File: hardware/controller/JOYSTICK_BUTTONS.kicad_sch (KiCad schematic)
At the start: 0 parts

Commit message: asdasd
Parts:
- added J2, J3: Joystick, SamacSys_Parts:SparkfunJoystick, symbol SamacSys_Parts:Joystick_Sparkfun_COM-09032
- added R1, R2, R3, R4, R5, R6: 10k, RESC2012X60N, symbol Device:R
- added SW1: UP, SamacSys_Parts:SW_PUSH_6mm, symbol ECE319K:SW_Push
- added SW2: LEFT, SamacSys_Parts:SW_PUSH_6mm, symbol ECE319K:SW_Push
- added SW3: DOWN, SamacSys_Parts:SW_PUSH_6mm, symbol ECE319K:SW_Push
- added SW4: RGHT, SamacSys_Parts:SW_PUSH_6mm, symbol ECE319K:SW_Push
- added SW5: BOOT, SamacSys_Parts:SW_PUSH_6mm, symbol Switch:SW_Push
- added SW6: RESET, SamacSys_Parts:SW_PUSH_6mm, symbol Switch:SW_Push
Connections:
- new net +3V3: J2.3 (V+), J2.4 (H+), J3.3 (V+), J3.4 (H+), SW1.2, SW2.2, SW3.2, SW4.2, SW5.2, SW6.2
- new net BUT_BOOT: R5.1, SW5.1
- new net BUT_DWN: R3.1, SW3.1
- new net BUT_LFT: R2.1, SW2.1
- new net BUT_RHT: R4.1, SW4.1
- new net BUT_RST: R6.1, SW6.1
- new net BUT_UP: R1.1, SW1.1
- new net GND: J2.1 (V-), J2.6 (H-), J3.1 (V-), J3.6 (H-), R1.2, R2.2, R3.2, R4.2, R5.2, R6.2
- new net JOY1_H: J2.5 (Hori)
- new net JOY1_V: J2.2 (Vert)
- new net JOY2_H: J3.5 (Hori)
- new net JOY2_V: J3.2 (Vert)
- no-connect marks 0 -> 4

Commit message: a
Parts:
- SW1, SW2, SW3, SW4: symbol ECE319K:SW_Push -> Switch:SW_Push
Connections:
- net BUT_DWN renamed BUT_DOWN
- net BUT_LFT renamed BUT_LEFT
- net BUT_RHT renamed BUT_RIGHT
- net BUT_RST renamed BUT_RESET

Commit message: fixed bus stuff
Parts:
- renumbered R1 to R3, R2 to R4, R3 to R5, R4 to R6, R5 to R7, R6 to R8
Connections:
- net BUT_BOOT renamed BUT_JOY.BUT_BOOT
- net BUT_DOWN renamed BUT_JOY.BUT_DOWN
- net BUT_LEFT renamed BUT_JOY.BUT_LEFT
- net BUT_RESET renamed BUT_JOY.BUT_RESET
- net BUT_RIGHT renamed BUT_JOY.BUT_RIGHT
- net BUT_UP renamed BUT_JOY.BUT_UP
- net JOY1_H renamed BUT_JOY.JOY1_H
- net JOY1_V renamed BUT_JOY.JOY1_V
- net JOY2_H renamed BUT_JOY.JOY2_H
- net JOY2_V renamed BUT_JOY.JOY2_V
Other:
- note added: "BOOT & RESET Buttons"
- note added: "Directional Buttons"
- note added: "Joysticks"
- moved on the sheet: J2, J3, R3, R4, R5, R6, R7, R8, SW1, SW2, SW3, SW4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

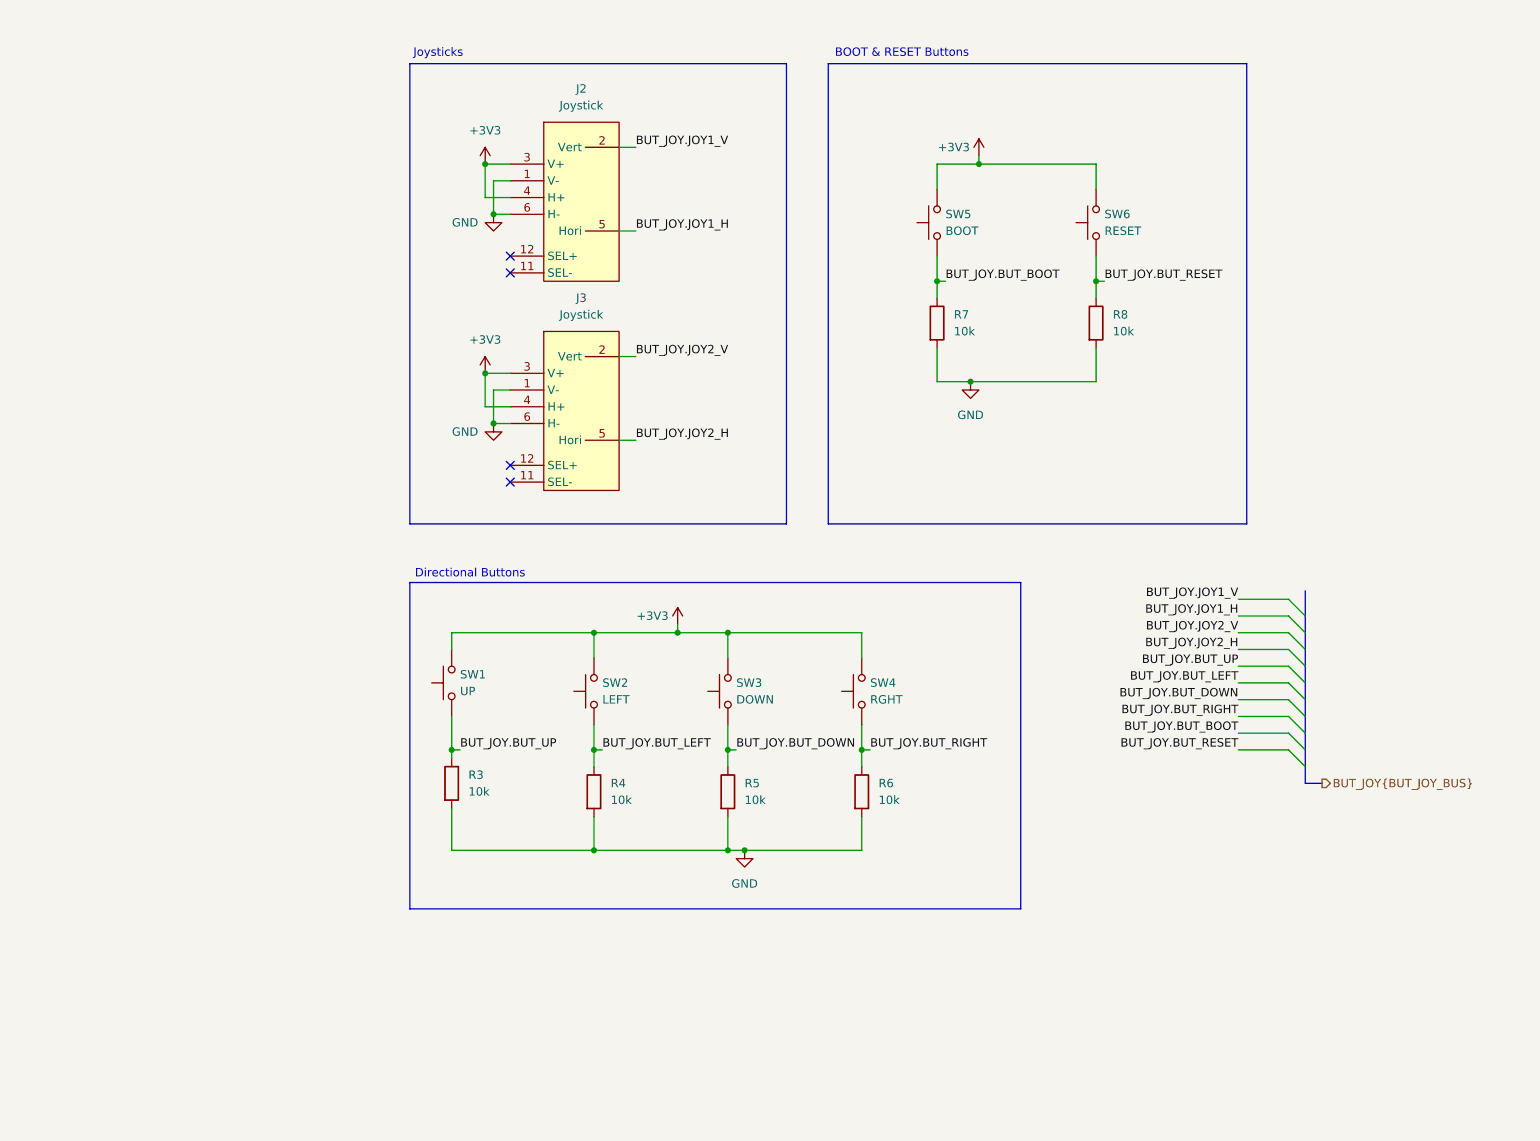
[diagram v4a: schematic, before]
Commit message: modified power circuitry
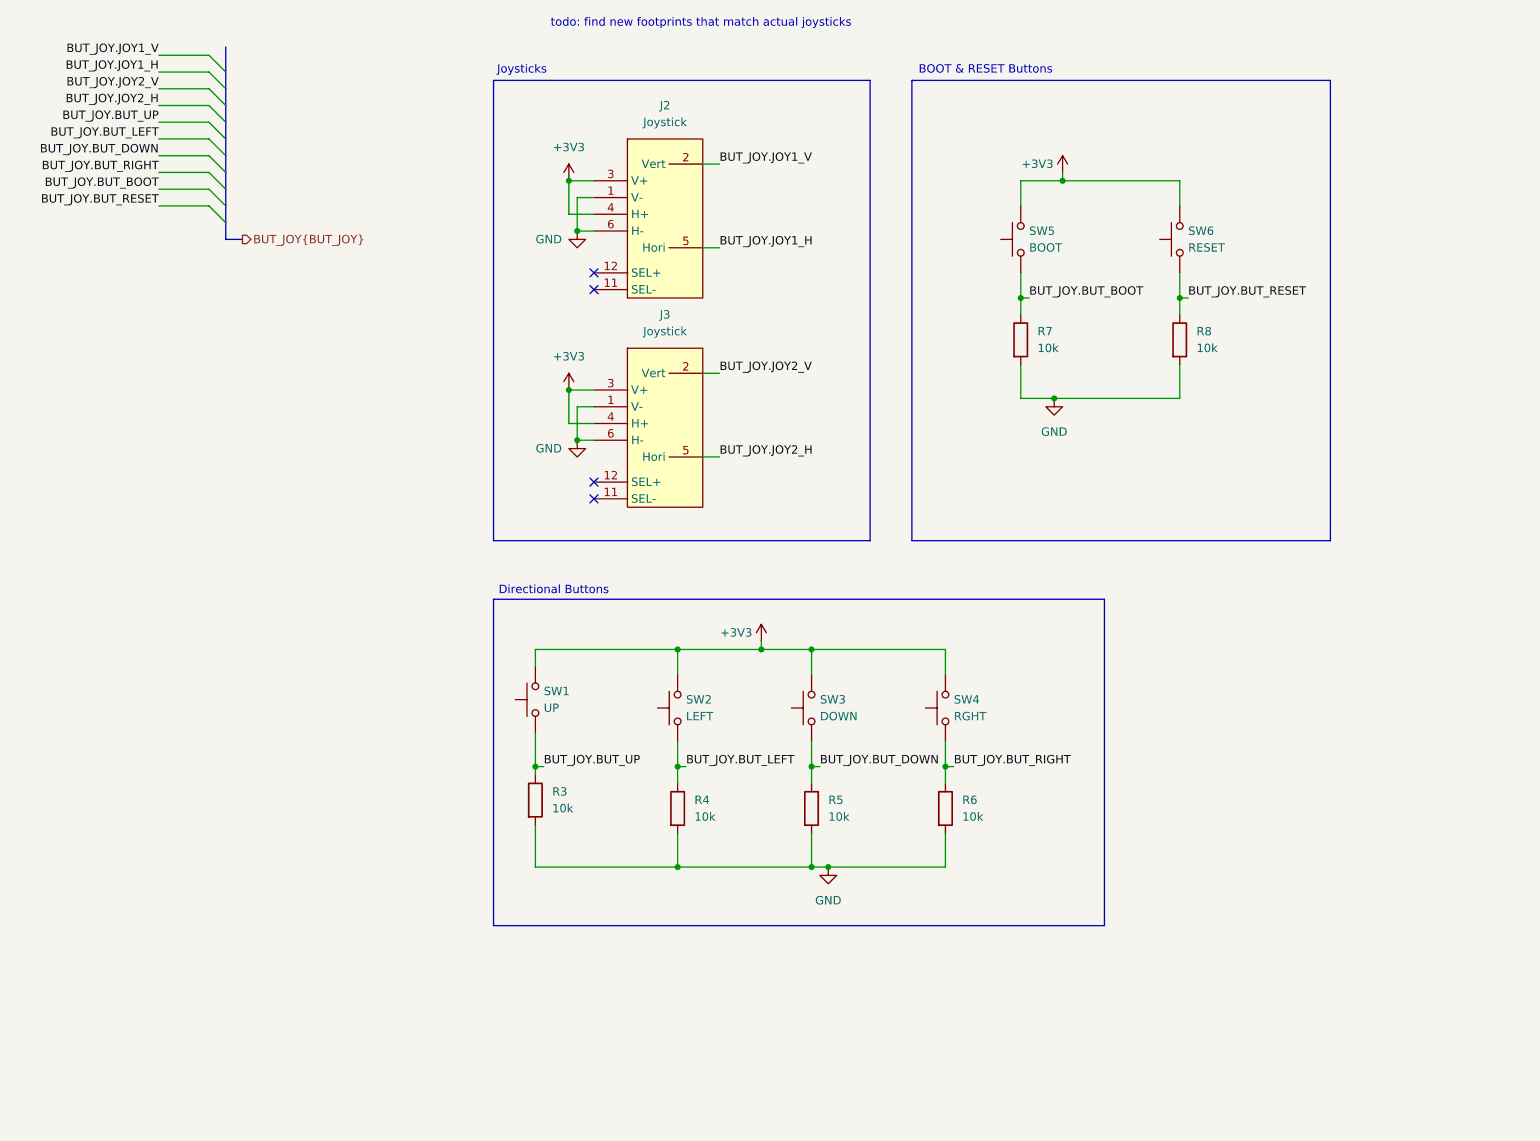
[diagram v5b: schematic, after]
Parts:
- R3, R4, R5, R6, R7, R8: footprint RESC2012X60N -> SamacSys_Parts:RESC2012X60N
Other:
- note added: "todo: find new footprints that match actual joysticks"
- moved on the sheet: J2, J3, R3, R4, R5, R6, R7, R8, SW1, SW2, SW3, SW4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

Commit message: finished first rev of controller schematic minus actually finding passive components. moved some features to rev2 todo
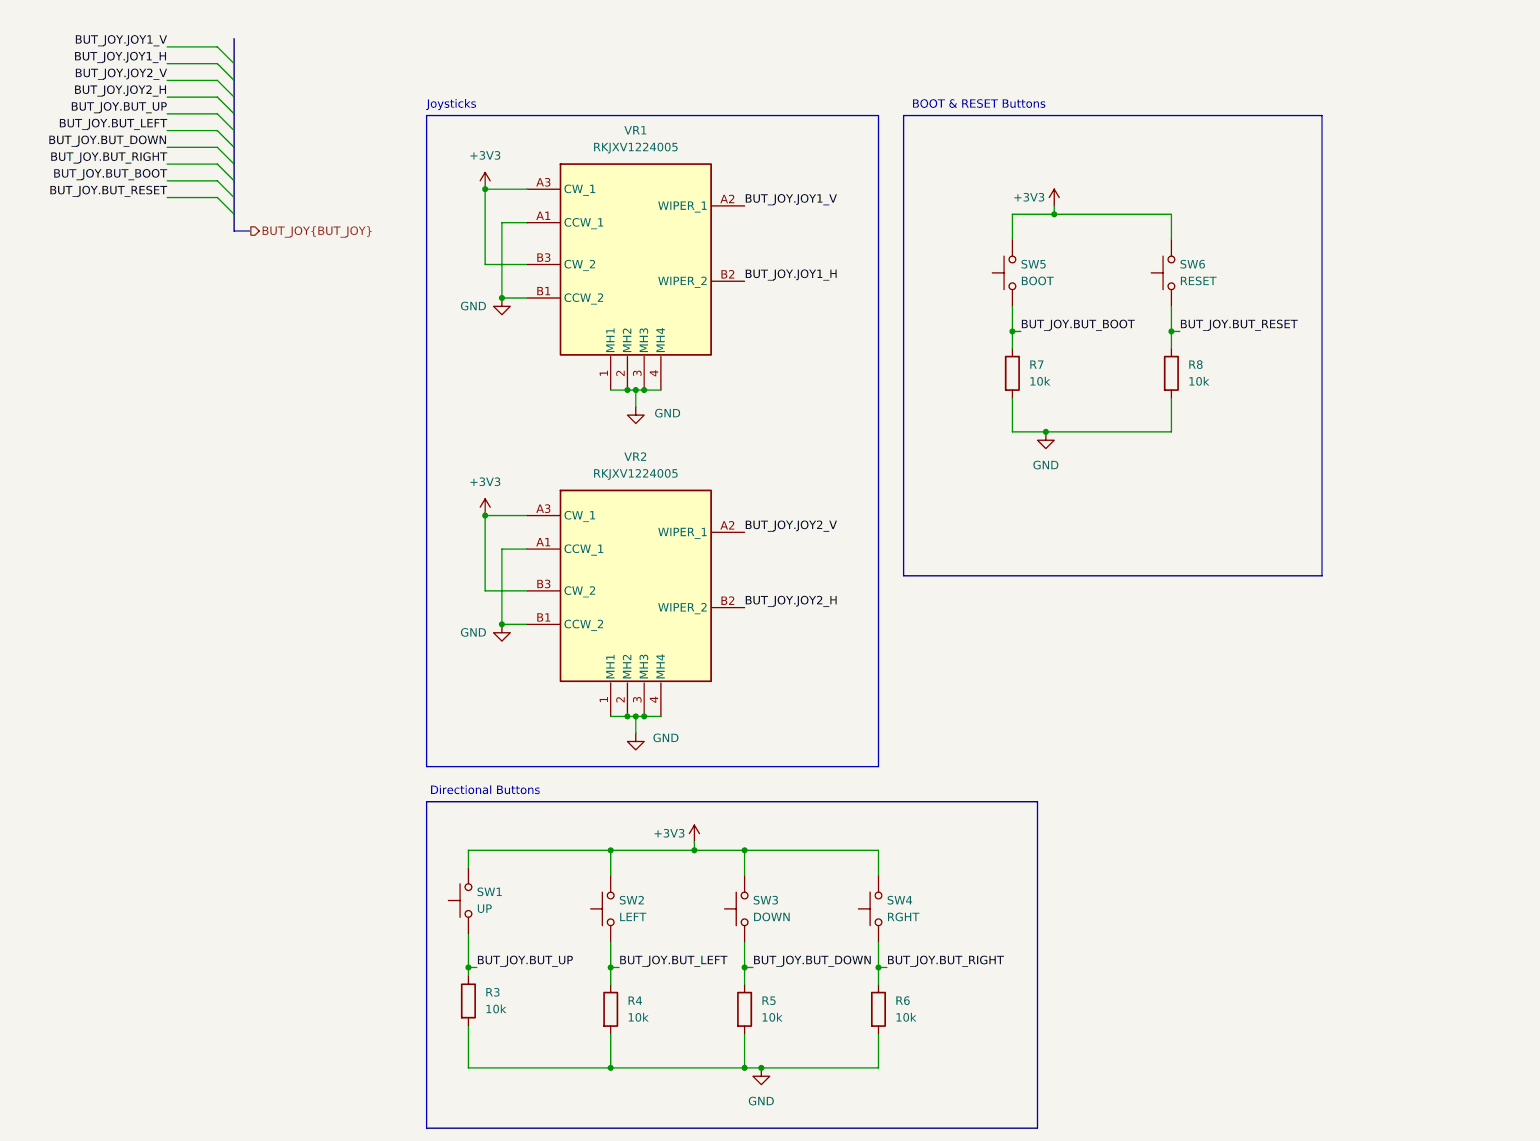
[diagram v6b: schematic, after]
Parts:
- removed J2, J3: Joystick, SamacSys_Parts:SparkfunJoystick, symbol SamacSys_Parts:Joystick_Sparkfun_COM-09032
- added VR1, VR2: RKJXV1224005, SamacSys_Parts:RKJXV1224005, symbol SamacSys_Parts:RKJXV1224005
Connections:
- net +3V3: now also VR1.A3 (CW_1), VR1.B3 (CW_2), VR2.A3 (CW_1), VR2.B3 (CW_2)
- net BUT_JOY.JOY1_H: now also VR1.B2 (WIPER_2)
- net BUT_JOY.JOY1_V: now also VR1.A2 (WIPER_1)
- net BUT_JOY.JOY2_H: now also VR2.B2 (WIPER_2)
- net BUT_JOY.JOY2_V: now also VR2.A2 (WIPER_1)
- net GND: now also VR1.1 (MH1), VR1.2 (MH2), VR1.3 (MH3), VR1.4 (MH4), VR1.A1 (CCW_1), VR1.B1 (CCW_2), VR2.1 (MH1), VR2.2 (MH2), VR2.3 (MH3), VR2.4 (MH4), VR2.A1 (CCW_1), VR2.B1 (CCW_2)
- no-connect marks 4 -> 0
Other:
- note removed: "todo: find new footprints that match actual joysticks"
- moved on the sheet: R3, R4, R5, R6, R7, R8, SW1, SW2, SW3, SW4, SW5, SW6

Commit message: Moved LEDs around. Replaced some discrete resistors with resistor arrays. Added mounting holes. Added. Added a lot of actual components for passive elements
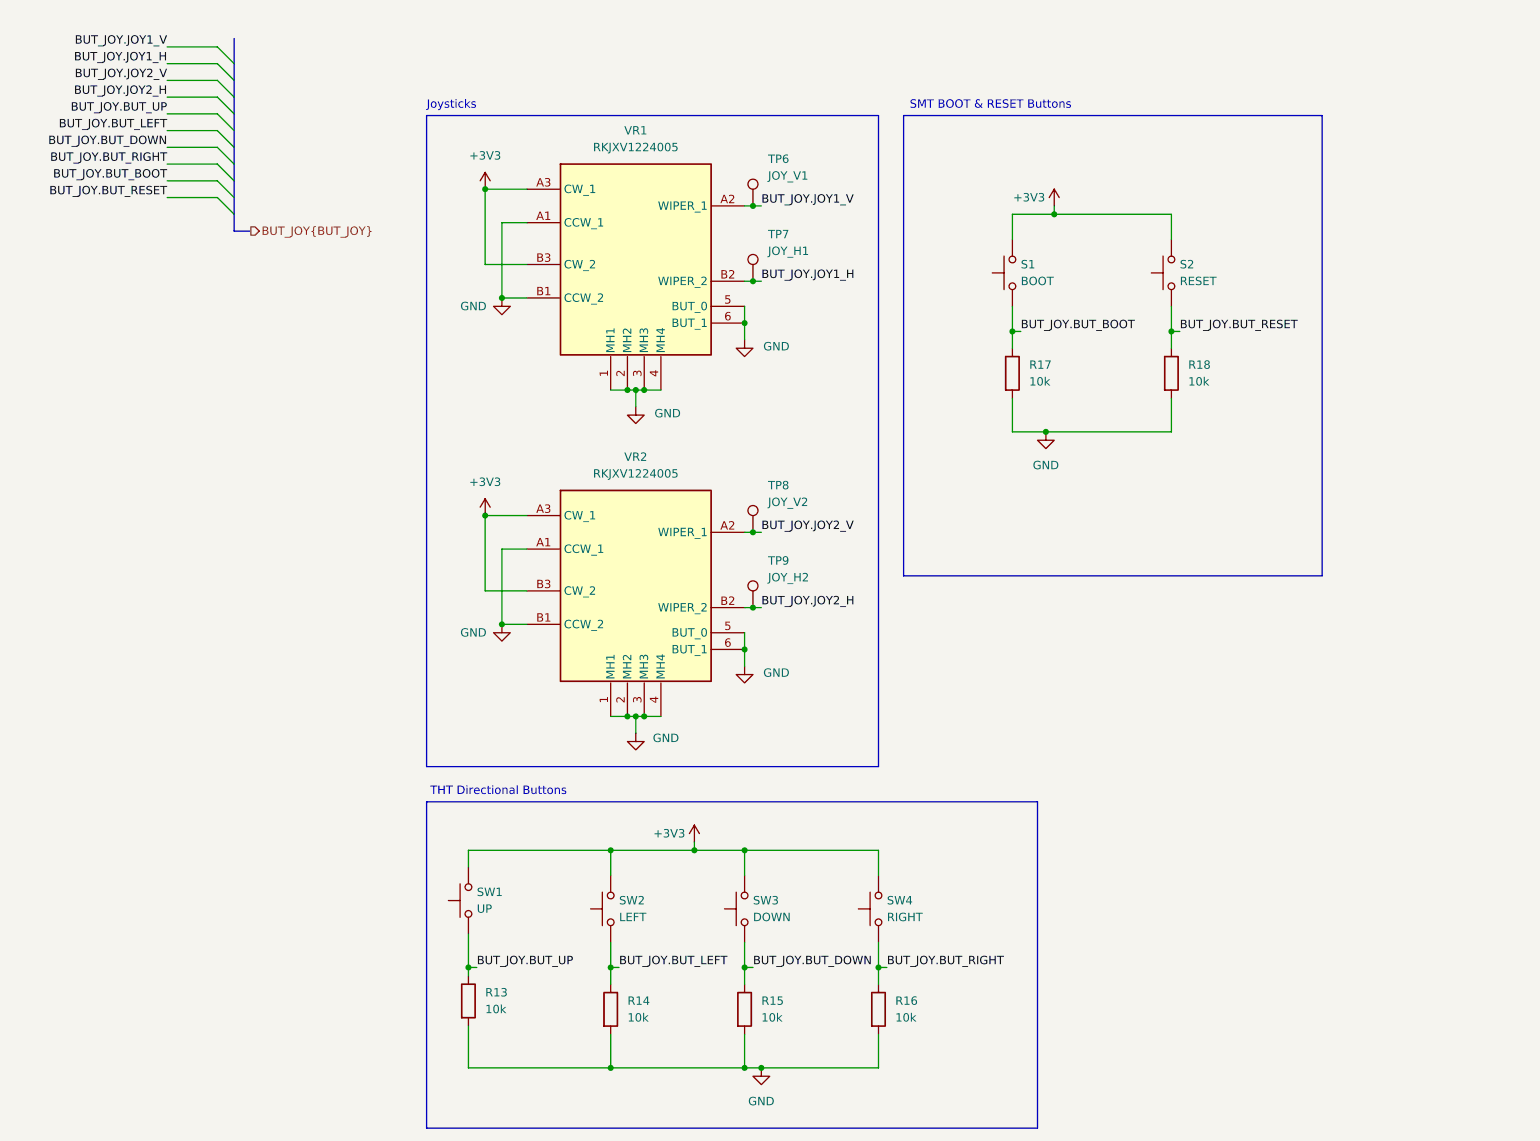
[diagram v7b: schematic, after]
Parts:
- removed SW5: BOOT, SamacSys_Parts:SW_PUSH_6mm, symbol Switch:SW_Push
- removed SW6: RESET, SamacSys_Parts:SW_PUSH_6mm, symbol Switch:SW_Push
- added S1: BOOT, TL1030AF500AQJ, symbol Switch:SW_Push
- added S2: RESET, TL1030AF500AQJ, symbol Switch:SW_Push
- added TP6: JOY_V1, TestPoint:TestPoint_Pad_1.0x1.0mm, symbol Connector:TestPoint
- added TP7: JOY_H1, TestPoint:TestPoint_Pad_1.0x1.0mm, symbol Connector:TestPoint
- added TP8: JOY_V2, TestPoint:TestPoint_Pad_1.0x1.0mm, symbol Connector:TestPoint
- added TP9: JOY_H2, TestPoint:TestPoint_Pad_1.0x1.0mm, symbol Connector:TestPoint
- R13: renamed from R3; footprint SamacSys_Parts:RESC2012X60N -> RESC2012X60N
- R14: renamed from R4; footprint SamacSys_Parts:RESC2012X60N -> RESC2012X60N
- R15: renamed from R5; footprint SamacSys_Parts:RESC2012X60N -> RESC2012X60N
- R16: renamed from R6; footprint SamacSys_Parts:RESC2012X60N -> RESC2012X60N
- R17: renamed from R7; footprint SamacSys_Parts:RESC2012X60N -> RESC2012X60N
- R18: renamed from R8; footprint SamacSys_Parts:RESC2012X60N -> RESC2012X60N
- SW4: value RGHT -> RIGHT
- VR1, VR2: footprint SamacSys_Parts:RKJXV1224005 -> RKJXV1224005
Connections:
- net +3V3: now also S1.2, S2.2
- net BUT_JOY.BUT_BOOT: now also S1.1
- net BUT_JOY.BUT_RESET: now also S2.1
- net BUT_JOY.JOY1_H: now also TP7.1
- net BUT_JOY.JOY1_V: now also TP6.1
- net BUT_JOY.JOY2_H: now also TP9.1
- net BUT_JOY.JOY2_V: now also TP8.1
- net GND: now also VR1.5 (BUT_0), VR1.6 (BUT_1), VR2.5 (BUT_0), VR2.6 (BUT_1)
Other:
- note added: "SMT BOOT & RESET Buttons"
- note added: "THT Directional Buttons"
- note removed: "BOOT & RESET Buttons"
- note removed: "Directional Buttons"
